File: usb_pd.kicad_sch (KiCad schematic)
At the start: 82 parts, among them Q1 Q_NMOS_DGS, Q2 Q_NMOS_DGS, Q3 Q_NMOS_DGS, Q4 Q_NMOS_DGS, U4 TPS5403DR, U5 BQ25731

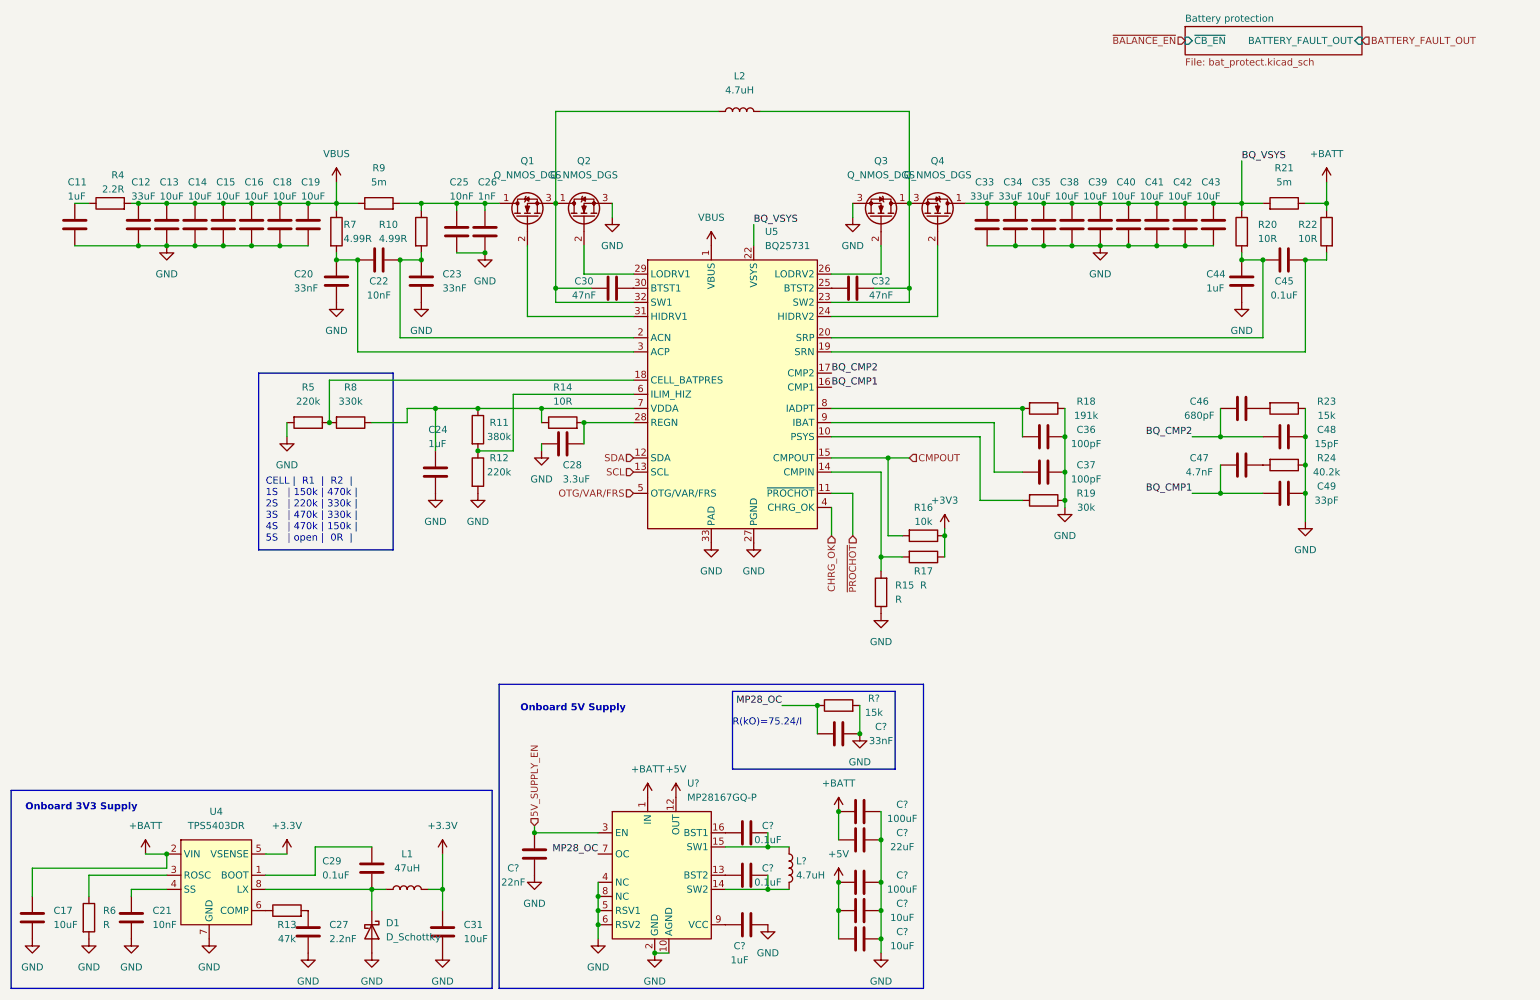
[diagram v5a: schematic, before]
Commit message: added adcin2 config description, fixed some rule check errors
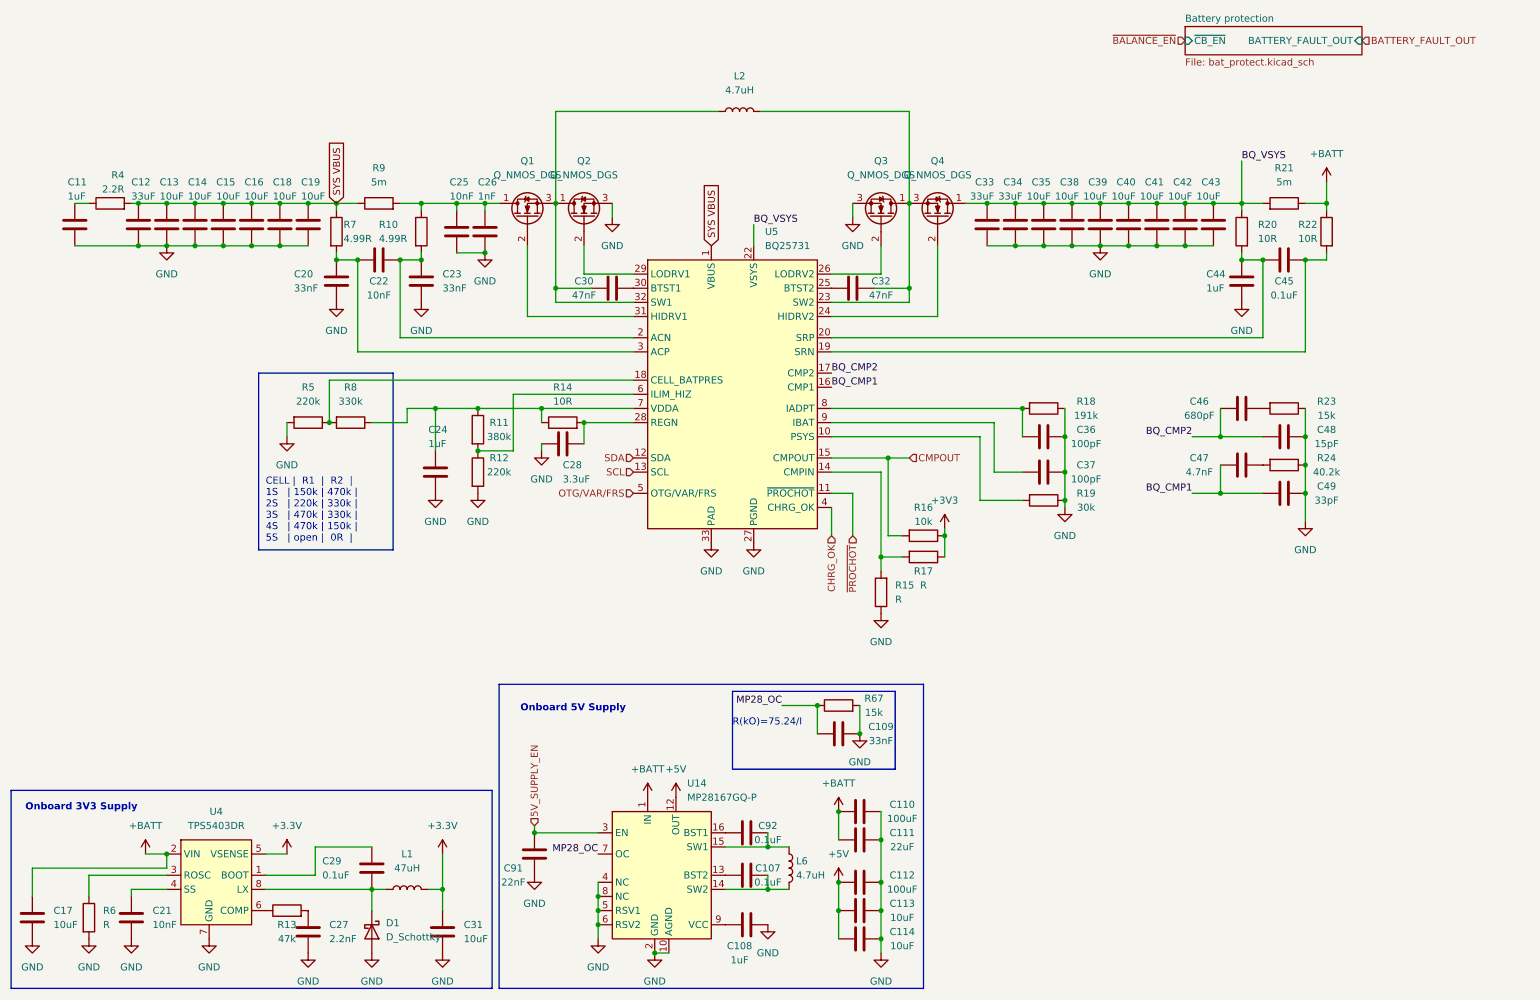
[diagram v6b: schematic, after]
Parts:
- gave numbers to parts that had none: 13
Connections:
- net VBUS renamed SYS VBUS
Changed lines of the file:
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@@
-    (stroke (width 0) (type default) (color 0 0 0 0))
-  )
-  (wire (pts (xy 71.12 50.8) (xy 71.12 54.61))
     (stroke (width 0) (type default) (color 0 0 0 0))
   )
@@
     (effects (font (size 1.27 1.27)) (justify left bottom))
   )
+  (global_label "SYS VBUS" (shape input) (at 138.43 62.23 90) (fields_autoplaced)
+    (effects (font (size 1.27 1.27)) (justify left))
+    (property "Intersheet References" "${INTERSHEET_REFS}" (id 0) (at 138.3506 50.4431 90)
+      (effects (font (size 1.27 1.27)) (justify left) hide)
+    )
+  )
+  (global_label "SYS VBUS" (shape input) (at 71.12 54.61 90) (fields_autoplaced)
+    (effects (font (size 1.27 1.27)) (justify left))
+    (property "Intersheet References" "${INTERSHEET_REFS}" (id 0) (at 71.0406 42.8231 90)
+      (effects (font (size 1.27 1.27)) (justify left) hide)
+    )
+  )
   (hierarchical_label "SCL" (shape input) (at 124.46 102.87 180)
     (effects (font (size 1.27 1.27)) (justify right))
@@
   (symbol (lib_id "Device:C") (at 144.78 175.26 90) (unit 1)
     (in_bom yes) (on_board yes)
-    (property "Reference" "C?" (id 0) (at 148.59 173.99 90))
+    (property "Reference" "C107" (id 0) (at 148.59 173.99 90))
     (property "Value" "0.1uF" (id 1) (at 148.59 176.53 90))
     (property "Footprint" "" (id 2) (at 148.59 174.2948 0)
@@
   (symbol (lib_id "power:GND") (at 165.1 149.86 0) (unit 1)
     (in_bom yes) (on_board yes) (fields_autoplaced)
-    (property "Reference" "#PWR?" (id 0) (at 165.1 156.21 0)
+    (property "Reference" "#PWR0259" (id 0) (at 165.1 156.21 0)
       (effects (font (size 1.27 1.27)) hide)
     )
@@
   (symbol (lib_id "power:GND") (at 168.91 189.23 0) (unit 1)
     (in_bom yes) (on_board yes) (fields_autoplaced)
-    (property "Reference" "#PWR?" (id 0) (at 168.91 195.58 0)
+    (property "Reference" "#PWR0210" (id 0) (at 168.91 195.58 0)
       (effects (font (size 1.27 1.27)) hide)
     )
@@
   (symbol (lib_id "power:+BATT") (at 127 161.29 0) (unit 1)
     (in_bom yes) (on_board yes) (fields_autoplaced)
-    (property "Reference" "#PWR?" (id 0) (at 127 165.1 0)
+    (property "Reference" "#PWR0214" (id 0) (at 127 165.1 0)
       (effects (font (size 1.27 1.27)) hide)
     )
@@
   (symbol (lib_id "Device:C") (at 165.1 163.83 90) (unit 1)
     (in_bom yes) (on_board yes)
-    (property "Reference" "C?" (id 0) (at 172.72 162.56 90))
+    (property "Reference" "C110" (id 0) (at 172.72 162.56 90))
     (property "Value" "100uF" (id 1) (at 172.72 165.1 90))
     (property "Footprint" "" (id 2) (at 168.91 162.8648 0)
@@
   (symbol (lib_id "power:+5V") (at 161.29 176.53 0) (unit 1)
     (in_bom yes) (on_board yes) (fields_autoplaced)
-    (property "Reference" "#PWR?" (id 0) (at 161.29 180.34 0)
+    (property "Reference" "#PWR0230" (id 0) (at 161.29 180.34 0)
       (effects (font (size 1.27 1.27)) hide)
     )
@@
   (symbol (lib_id "power:GND") (at 118.11 186.69 0) (unit 1)
     (in_bom yes) (on_board yes) (fields_autoplaced)
-    (property "Reference" "#PWR?" (id 0) (at 118.11 193.04 0)
+    (property "Reference" "#PWR0218" (id 0) (at 118.11 193.04 0)
       (effects (font (size 1.27 1.27)) hide)
     )
@@
   (symbol (lib_id "Device:L") (at 152.4 173.99 0) (unit 1)
     (in_bom yes) (on_board yes) (fields_autoplaced)
-    (property "Reference" "L?" (id 0) (at 153.67 172.7199 0)
+    (property "Reference" "L6" (id 0) (at 153.67 172.7199 0)
       (effects (font (size 1.27 1.27)) (justify left))
     )
@@
   (symbol (lib_id "power:+5V") (at 132.08 161.29 0) (unit 1)
     (in_bom yes) (on_board yes) (fields_autoplaced)
-    (property "Reference" "#PWR?" (id 0) (at 132.08 165.1 0)
+    (property "Reference" "#PWR0211" (id 0) (at 132.08 165.1 0)
       (effects (font (size 1.27 1.27)) hide)
     )
@@
   (symbol (lib_id "airsoft_controller:MP28167GQ-P") (at 129.54 175.26 0) (unit 1)
     (in_bom yes) (on_board yes) (fields_autoplaced)
-    (property "Reference" "U?" (id 0) (at 134.0994 158.75 0)
+    (property "Reference" "U14" (id 0) (at 134.0994 158.75 0)
       (effects (font (size 1.27 1.27)) (justify left))
     )
@@
   (symbol (lib_id "Device:C") (at 165.1 176.53 90) (unit 1)
     (in_bom yes) (on_board yes)
-    (property "Reference" "C?" (id 0) (at 172.72 175.26 90))
+    (property "Reference" "C112" (id 0) (at 172.72 175.26 90))
     (property "Value" "100uF" (id 1) (at 172.72 177.8 90))
     (property "Footprint" "" (id 2) (at 168.91 175.5648 0)
@@
   (symbol (lib_id "power:GND") (at 128.27 189.23 0) (unit 1)
     (in_bom yes) (on_board yes) (fields_autoplaced)
-    (property "Reference" "#PWR?" (id 0) (at 128.27 195.58 0)
+    (property "Reference" "#PWR0215" (id 0) (at 128.27 195.58 0)
       (effects (font (size 1.27 1.27)) hide)
     )
@@
   (symbol (lib_id "Device:C") (at 106.68 171.45 180) (unit 1)
     (in_bom yes) (on_board yes)
-    (property "Reference" "C?" (id 0) (at 102.87 173.99 0))
+    (property "Reference" "C91" (id 0) (at 102.87 173.99 0))
     (property "Value" "22nF" (id 1) (at 102.87 176.53 0))
     (property "Footprint" "" (id 2) (at 105.7148 167.64 0)
@@
     (pin "2")
   )
-  (symbol (lib_id "power:VBUS") (at 138.43 62.23 0) (unit 1)
-    (in_bom yes) (on_board yes) (fields_autoplaced)
-    (property "Reference" "#PWR0121" (id 0) (at 138.43 66.04 0)
-      (effects (font (size 1.27 1.27)) hide)
-    )
-    (property "Value" "VBUS" (id 1) (at 138.43 57.15 0))
-    (property "Footprint" "" (id 2) (at 138.43 62.23 0)
-      (effects (font (size 1.27 1.27)) hide)
-    )
-    (property "Datasheet" "" (id 3) (at 138.43 62.23 0)
-      (effects (font (size 1.27 1.27)) hide)
-    )
-    (pin "1")
-  )
   (symbol (lib_id "Device:C") (at 165.1 168.91 90) (unit 1)
     (in_bom yes) (on_board yes)
-    (property "Reference" "C?" (id 0) (at 172.72 167.64 90))
+    (property "Reference" "C111" (id 0) (at 172.72 167.64 90))
     (property "Value" "22uF" (id 1) (at 172.72 170.18 90))
     (property "Footprint" "" (id 2) (at 168.91 167.9448 0)
@@
   (symbol (lib_id "Device:R") (at 161.29 144.78 90) (unit 1)
     (in_bom yes) (on_board yes)
-    (property "Reference" "R?" (id 0) (at 167.64 143.51 90))
+    (property "Reference" "R67" (id 0) (at 167.64 143.51 90))
     (property "Value" "15k" (id 1) (at 167.64 146.05 90))
     (property "Footprint" "" (id 2) (at 161.29 146.558 90)
@@
   (symbol (lib_id "Device:C") (at 161.29 149.86 90) (unit 1)
     (in_bom yes) (on_board yes)
-    (property "Reference" "C?" (id 0) (at 168.91 148.59 90))
+    (property "Reference" "C109" (id 0) (at 168.91 148.59 90))
     (property "Value" "33nF" (id 1) (at 168.91 151.13 90))
     (property "Footprint" "" (id 2) (at 165.1 148.8948 0)
@@
   (symbol (lib_id "power:+BATT") (at 161.29 163.83 0) (unit 1)
     (in_bom yes) (on_board yes) (fields_autoplaced)
-    (property "Reference" "#PWR?" (id 0) (at 161.29 167.64 0)
+    (property "Reference" "#PWR0249" (id 0) (at 161.29 167.64 0)
       (effects (font (size 1.27 1.27)) hide)
     )
@@
   (symbol (lib_id "Device:C") (at 144.78 184.15 90) (unit 1)
     (in_bom yes) (on_board yes)
-    (property "Reference" "C?" (id 0) (at 143.51 187.96 90))
+    (property "Reference" "C108" (id 0) (at 143.51 187.96 90))
     (property "Value" "1uF" (id 1) (at 143.51 190.5 90))
     (property "Footprint" "" (id 2) (at 148.59 183.1848 0)
@@
   (symbol (lib_id "power:+3.3V") (at 62.23 171.45 0) (unit 1)
     (in_bom yes) (on_board yes) (fields_autoplaced)
-    (property "Reference" "#PWR?" (id 0) (at 62.23 175.26 0)
+    (property "Reference" "#PWR0221" (id 0) (at 62.23 175.26 0)
       (effects (font (size 1.27 1.27)) hide)
     )
@@
   (symbol (lib_id "Device:C") (at 144.78 167.64 90) (unit 1)
     (in_bom yes) (on_board yes)
-    (property "Reference" "C?" (id 0) (at 148.59 166.37 90))
+    (property "Reference" "C92" (id 0) (at 148.59 166.37 90))
     (property "Value" "0.1uF" (id 1) (at 148.59 168.91 90))
     (property "Footprint" "" (id 2) (at 148.59 166.6748 0)
@@
     (pin "2")
   )
-  (symbol (lib_id "power:VBUS") (at 71.12 50.8 0) (unit 1)
-    (in_bom yes) (on_board yes) (fields_autoplaced)
-    (property "Reference" "#PWR0132" (id 0) (at 71.12 54.61 0)
-      (effects (font (size 1.27 1.27)) hide)
-    )
-    (property "Value" "VBUS" (id 1) (at 71.12 45.72 0))
-    (property "Footprint" "" (id 2) (at 71.12 50.8 0)
-      (effects (font (size 1.27 1.27)) hide)
-    )
-    (property "Datasheet" "" (id 3) (at 71.12 50.8 0)
-      (effects (font (size 1.27 1.27)) hide)
-    )
-    (pin "1")
-  )
   (symbol (lib_id "Device:C") (at 45.72 58.42 180) (unit 1)
     (in_bom yes) (on_board yes)
@@
   (symbol (lib_id "power:GND") (at 106.68 175.26 0) (unit 1)
     (in_bom yes) (on_board yes) (fields_autoplaced)
-    (property "Reference" "#PWR?" (id 0) (at 106.68 181.61 0)
+    (property "Reference" "#PWR0219" (id 0) (at 106.68 181.61 0)
       (effects (font (size 1.27 1.27)) hide)
     )
@@
   (symbol (lib_id "Device:C") (at 165.1 186.69 90) (unit 1)
     (in_bom yes) (on_board yes)
-    (property "Reference" "C?" (id 0) (at 172.72 185.42 90))
+    (property "Reference" "C114" (id 0) (at 172.72 185.42 90))
     (property "Value" "10uF" (id 1) (at 172.72 187.96 90))
     (property "Footprint" "" (id 2) (at 168.91 185.7248 0)
@@
   (symbol (lib_id "Device:C") (at 165.1 181.61 90) (unit 1)
     (in_bom yes) (on_board yes)
-    (property "Reference" "C?" (id 0) (at 172.72 180.34 90))
+    (property "Reference" "C113" (id 0) (at 172.72 180.34 90))
     (property "Value" "10uF" (id 1) (at 172.72 182.88 90))
     (property "Footprint" "" (id 2) (at 168.91 180.6448 0)
@@
   (symbol (lib_id "power:GND") (at 148.59 184.15 0) (unit 1)
     (in_bom yes) (on_board yes) (fields_autoplaced)
-    (property "Reference" "#PWR?" (id 0) (at 148.59 190.5 0)
-      (effects (font (size 1.27 1.27)) hide)
-    )
+    (property "Reference" "#PWR0209" (id 0) (at 148.59 190.5 0)
+      (effects (font (size 1.27 1.27)) hide)
+    )

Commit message: minor optimized pinassignement, added capacitors, added connectors
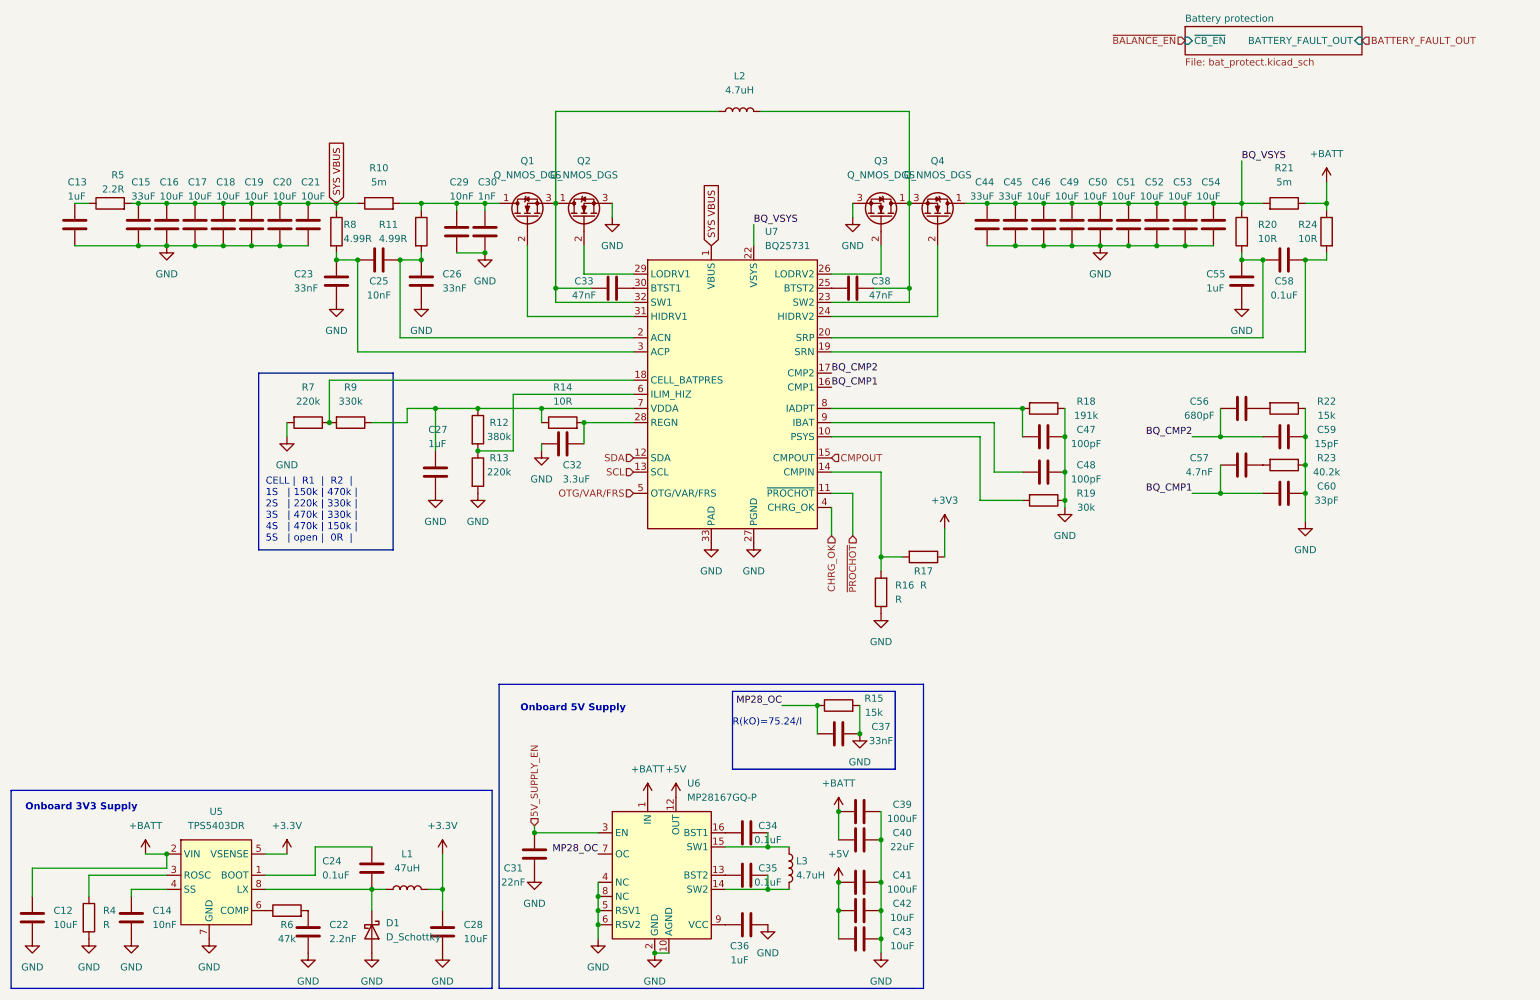
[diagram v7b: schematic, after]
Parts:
- removed R16: 10k, symbol Device:R
- renumbered C17 to C12, C11 to C13, C21 to C14, C12 to C15, C13 to C16, C14 to C17, C15 to C18, C16 to C19, C18 to C20, C19 to C21, C27 to C22, C20 to C23, C29 to C24, C22 to C25, C23 to C26, C24 to C27, C31 to C28, C25 to C29, C26 to C30, C91 to C31, C28 to C32, C30 to C33, C92 to C34, C107 to C35, C108 to C36, C109 to C37, C32 to C38, C110 to C39, C111 to C40, C112 to C41, C113 to C42, C114 to C43, C33 to C44, C34 to C45, C35 to C46, C36 to C47, C37 to C48, C38 to C49, C39 to C50, C40 to C51, C41 to C52, C42 to C53, C43 to C54, C44 to C55, C46 to C56, C47 to C57, C45 to C58, C48 to C59, C49 to C60, L6 to L3, R9 to R10, R10 to R11, R11 to R12, R12 to R13, R67 to R15, R15 to R16, R23 to R22, R24 to R23, R22 to R24, R6 to R4, R4 to R5, R13 to R6, R5 to R7, R7 to R8, R8 to R9, U4 to U5, U14 to U6, U5 to U7
